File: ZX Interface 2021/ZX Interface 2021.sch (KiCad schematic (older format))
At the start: 44 parts, among them J1 AJS #1, J2 AJS #2, J3 SWAP_ROMS, J4 Cartridge, SW1 RESET, U1 74LS245, U2 74LS245, U3 74LS27, U4 74LS04, U5 27C512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

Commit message: Created proper extended cartridge symbols
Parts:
- removed U5: 27C512, Package_DIP:DIP-28_W15.24mm, symbol Memory_EPROM:27C512
- added M1, M2, M3, M4, M5, M6: Mounting, symbol mounting:Mounting
- J3: footprint (none) -> Connector_PinHeader_2.54mm:PinHeader_2x02_P2.54mm_Vertical
- J4: footprint (none) -> zx_spectrum:ZX_Spectrum_Cartridge_Port; symbol Connector_Generic:Conn_02x22_Row_Letter_Last -> zx_spectrum:cartridge_port
- U1, U2, U6: footprint (none) -> Package_DIP:DIP-20_W7.62mm_Socket_LongPads
- U3, U4: footprint (none) -> Package_DIP:DIP-14_W7.62mm_Socket_LongPads
- U7, U8: footprint (none) -> Package_DIP:DIP-16_W7.62mm_Socket_LongPads
- Z1: value ZXBUS -> ZX Spectrum; footprint (none) -> zx_spectrum:ZX_Spectrum_Expansion_Right_Angle; symbol zxbus:ZXBUS -> zx_spectrum:expansion_port
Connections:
- net labels added: EXROM, OUT_31, OUT_63
- net labels removed: Port_31, ~EXROM
- wire segments 297 -> 279
- no-connect marks 58 -> 48
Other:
- note added: "/ROM_CS is an enable for\nthe internal ZX Spectrum\nROM. Bring high to use\ncartridge."
- note added: "Sinclair Interface 2 joystick interface, but with\nAtari-style pinout (because noone wants to use\nan SJS or even have one that works properly)."
- moved on the sheet: R12, U4E

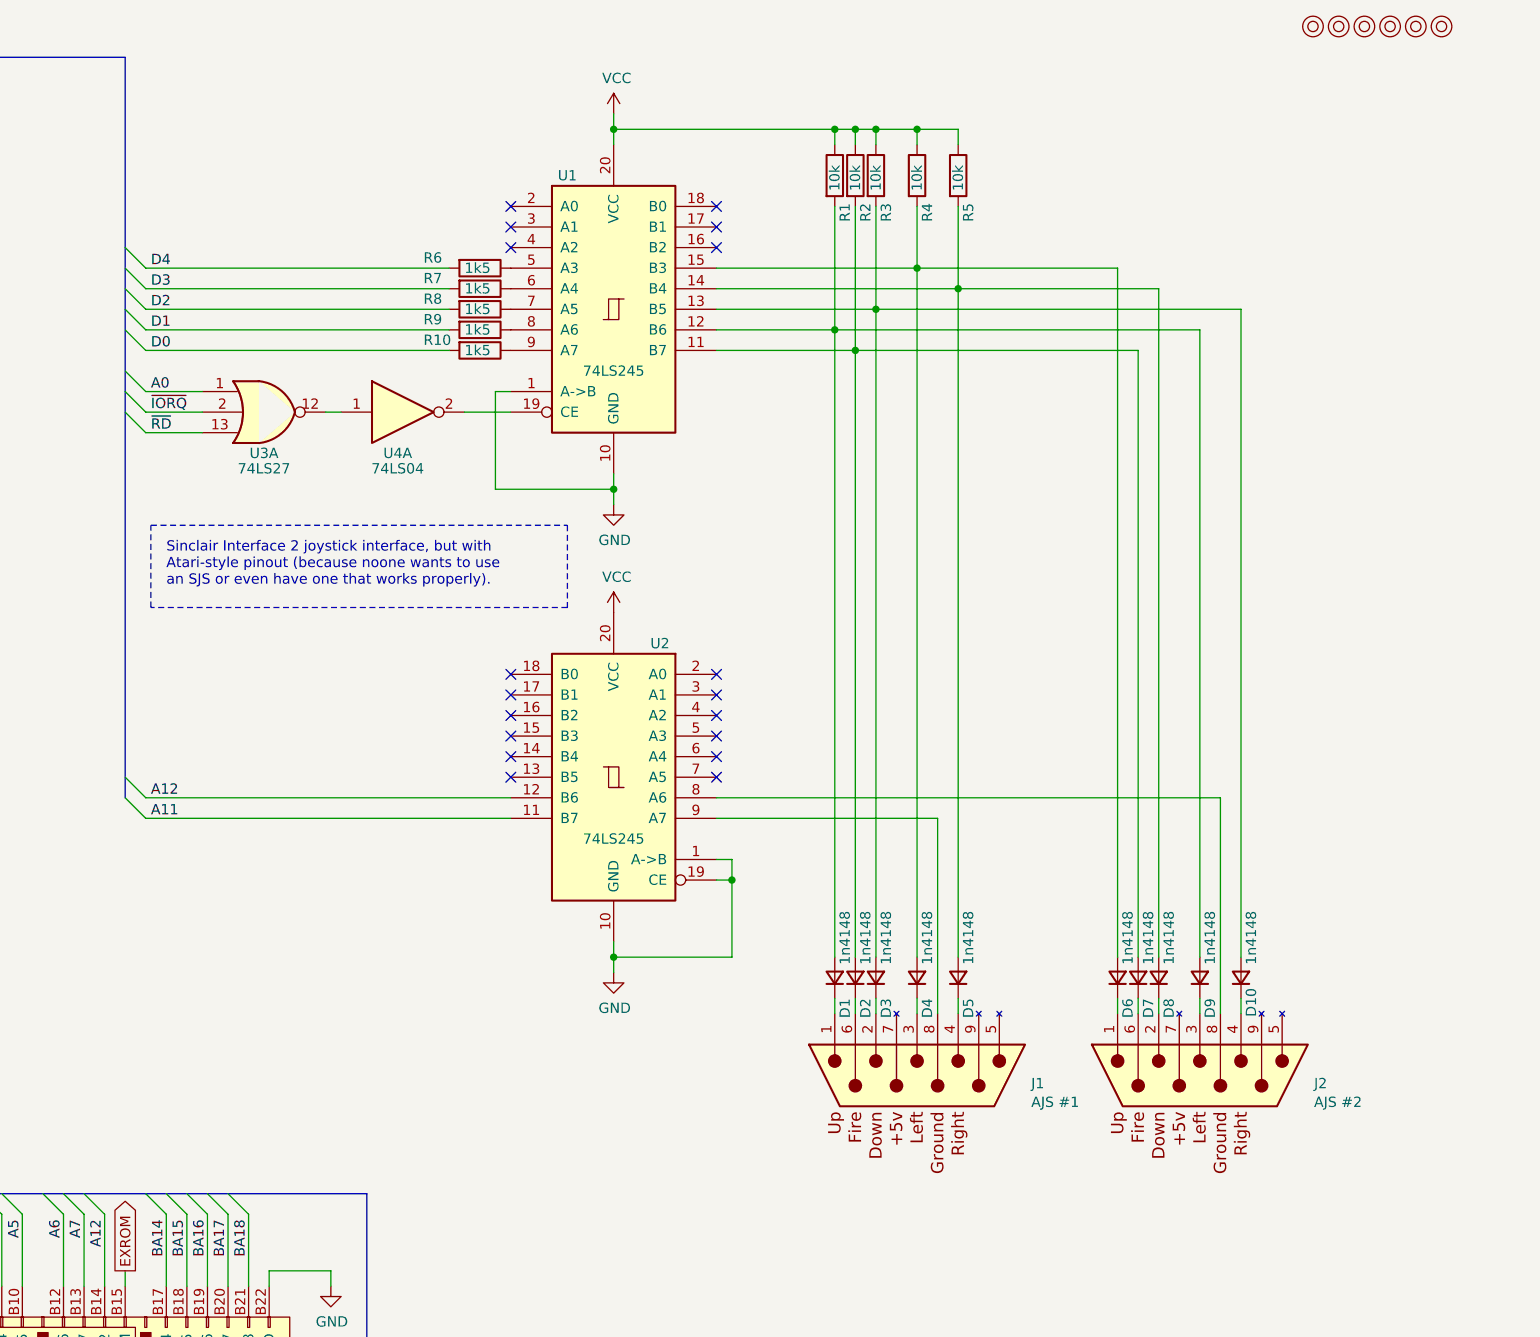
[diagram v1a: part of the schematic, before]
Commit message: Assigned footprints
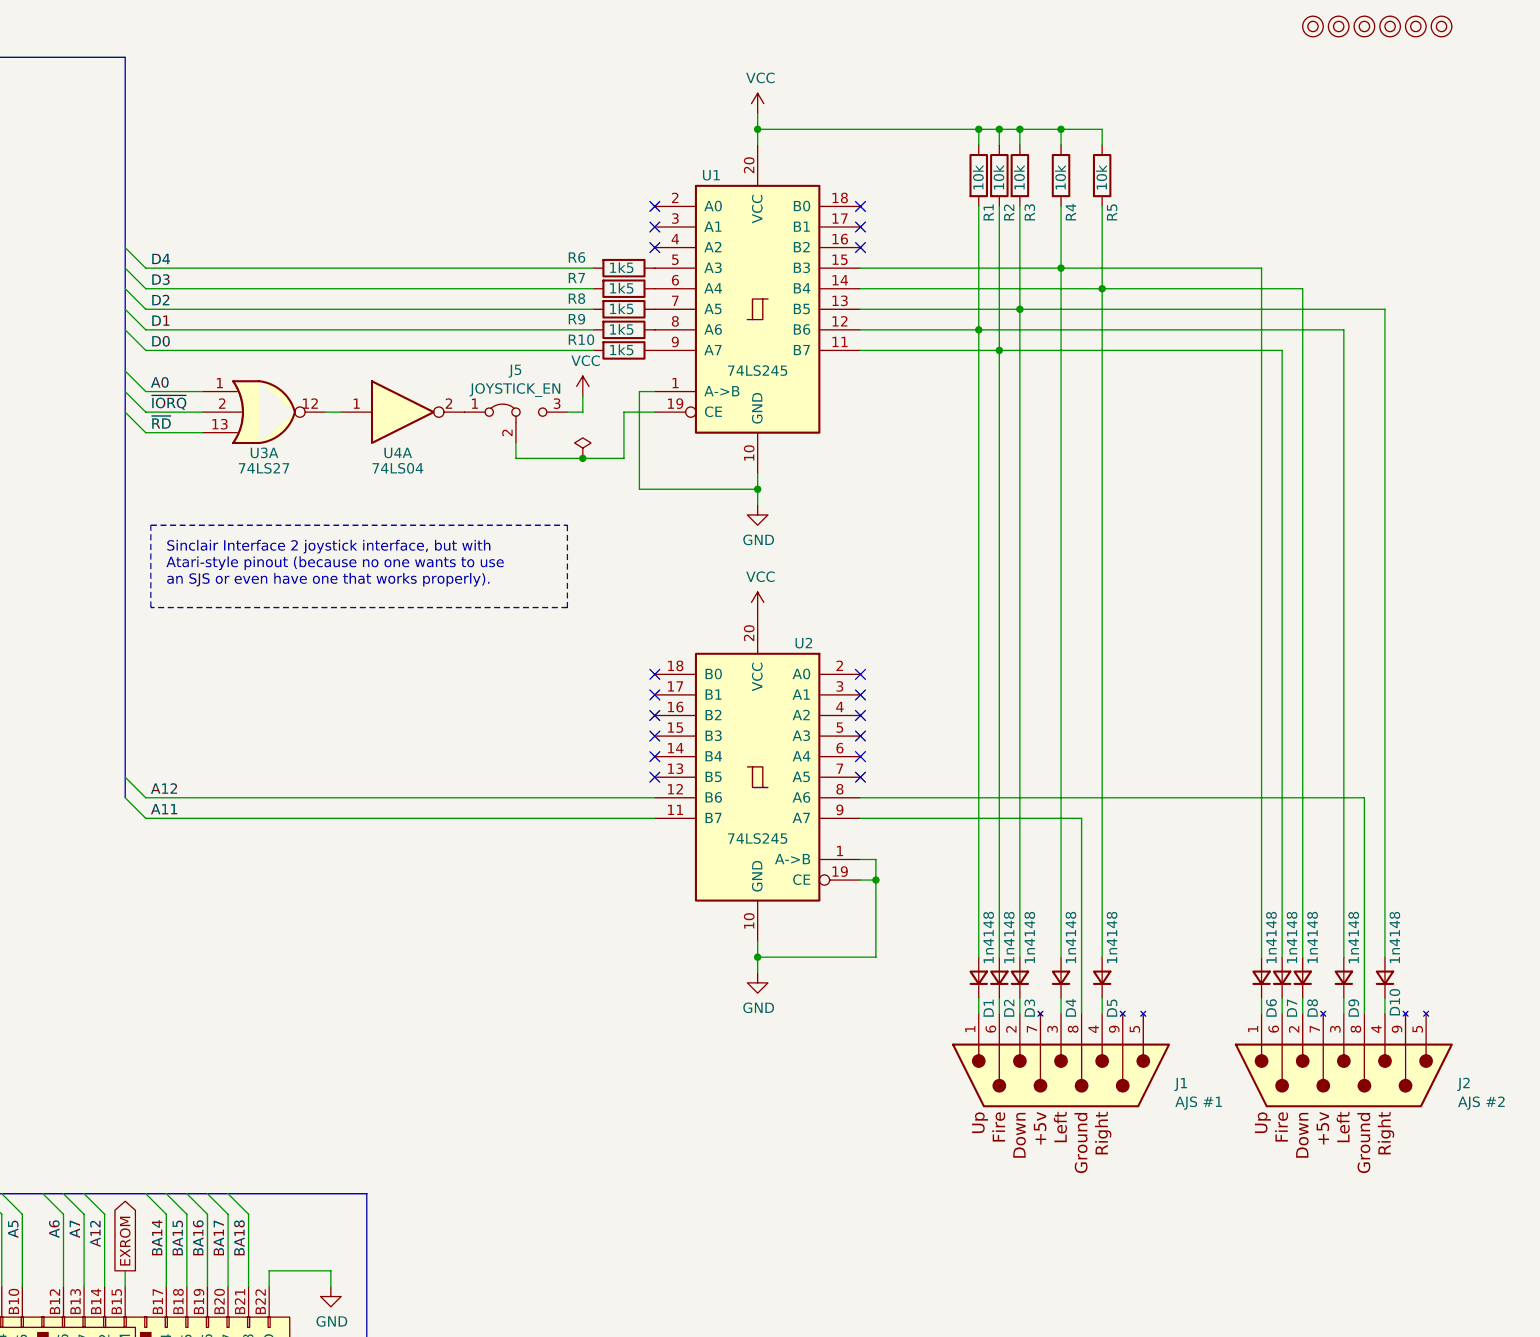
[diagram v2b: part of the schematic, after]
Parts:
- added J5: JOYSTICK_EN, Connector_PinHeader_2.54mm:PinHeader_1x03_P2.54mm_Vertical, symbol Jumper:Jumper_3_Bridged12
- D1, D10, D2, D3, D4, D5, D6, D7, D8, D9: footprint (none) -> Diode_THT:D_DO-35_SOD27_P7.62mm_Horizontal
- J1, J2: footprint (none) -> RND_DSUB:DSUB-9_Male_Vertical_Pitch2.77x2.84mm
- M1, M2, M3, M4, M5, M6: footprint (none) -> mounting:M3_pin
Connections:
- net VCC: now also J5.3 (B)
- net at U1.19 (CE): now also J5.2 (C); no longer U4.2
- new net: J5.1 (A), U4.2
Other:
- note added: "Sinclair Interface 2 joystick interface, but with\nAtari-style pinout (because no one wants to use\nan SJS or even have one that works properly)."
- note removed: "Sinclair Interface 2 joystick interface, but with\nAtari-style pinout (because noone wants to use\nan SJS or even have one that works properly)."
- moved on the sheet: D1, D10, D2, D3, D4, D5, D6, D7, D8, D9, J1, J2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

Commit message: Laying some tracks...
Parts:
- D1, D10, D2, D3, D4, D5, D6, D7, D8, D9: footprint Diode_THT:D_DO-35_SOD27_P7.62mm_Horizontal -> 1n4148:D_DO-35_SOD27_P7.62mm_Horizontal
- SW1: footprint Button_Switch_THT:SW_PUSH_6mm_H13mm -> switch_cutout:SW_PUSH_6mm
- Z1: footprint zx_spectrum:ZX_Spectrum_Expansion_Right_Angle -> zx_spectrum:ZX_Spectrum_Expansion_Edge
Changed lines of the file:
@@
 F 0 "Z1" H 2400 7776 39  0000 C CNN
 F 1 "ZX Spectrum" H 2400 7701 39  0000 C CNN
-F 2 "zx_spectrum:ZX_Spectrum_Expansion_Right_Angle" H 2050 4375 39  0001 C CNN
+F 2 "zx_spectrum:ZX_Spectrum_Expansion_Edge" H 2050 4375 39  0001 C CNN
 F 3 "" H 2050 4375 39  0001 C CNN
 	1    2050 4375
@@
 F 0 "D1" H 13625 5125 50  0000 R CNN
 F 1 "1n4148" H 14050 5125 50  0000 R CNN
-F 2 "Diode_THT:D_DO-35_SOD27_P7.62mm_Horizontal" V 13725 5175 50  0001 C CNN
+F 2 "1n4148:D_DO-35_SOD27_P7.62mm_Horizontal" V 13725 5175 50  0001 C CNN
 F 3 "~" V 13725 5175 50  0001 C CNN
 	1    13725 5175
@@
 F 0 "D2" H 13725 5125 50  0000 R CNN
 F 1 "1n4148" H 14150 5125 50  0000 R CNN
-F 2 "Diode_THT:D_DO-35_SOD27_P7.62mm_Horizontal" V 13825 5175 50  0001 C CNN
+F 2 "1n4148:D_DO-35_SOD27_P7.62mm_Horizontal" V 13825 5175 50  0001 C CNN
 F 3 "~" V 13825 5175 50  0001 C CNN
 	1    13825 5175
@@
 F 0 "D3" H 13825 5125 50  0000 R CNN
 F 1 "1n4148" H 14250 5125 50  0000 R CNN
-F 2 "Diode_THT:D_DO-35_SOD27_P7.62mm_Horizontal" V 13925 5175 50  0001 C CNN
+F 2 "1n4148:D_DO-35_SOD27_P7.62mm_Horizontal" V 13925 5175 50  0001 C CNN
 F 3 "~" V 13925 5175 50  0001 C CNN
 	1    13925 5175
@@
 F 0 "D4" H 14025 5125 50  0000 R CNN
 F 1 "1n4148" H 14450 5125 50  0000 R CNN
-F 2 "Diode_THT:D_DO-35_SOD27_P7.62mm_Horizontal" V 14125 5175 50  0001 C CNN
+F 2 "1n4148:D_DO-35_SOD27_P7.62mm_Horizontal" V 14125 5175 50  0001 C CNN
 F 3 "~" V 14125 5175 50  0001 C CNN
 	1    14125 5175
@@
 F 0 "D5" H 14225 5125 50  0000 R CNN
 F 1 "1n4148" H 14650 5125 50  0000 R CNN
-F 2 "Diode_THT:D_DO-35_SOD27_P7.62mm_Horizontal" V 14325 5175 50  0001 C CNN
+F 2 "1n4148:D_DO-35_SOD27_P7.62mm_Horizontal" V 14325 5175 50  0001 C CNN
 F 3 "~" V 14325 5175 50  0001 C CNN
 	1    14325 5175
@@
 F 0 "D6" H 15000 5125 50  0000 R CNN
 F 1 "1n4148" H 15425 5125 50  0000 R CNN
-F 2 "Diode_THT:D_DO-35_SOD27_P7.62mm_Horizontal" V 15100 5175 50  0001 C CNN
+F 2 "1n4148:D_DO-35_SOD27_P7.62mm_Horizontal" V 15100 5175 50  0001 C CNN
 F 3 "~" V 15100 5175 50  0001 C CNN
 	1    15100 5175
@@
 F 0 "D7" H 15100 5125 50  0000 R CNN
 F 1 "1n4148" H 15525 5125 50  0000 R CNN
-F 2 "Diode_THT:D_DO-35_SOD27_P7.62mm_Horizontal" V 15200 5175 50  0001 C CNN
+F 2 "1n4148:D_DO-35_SOD27_P7.62mm_Horizontal" V 15200 5175 50  0001 C CNN
 F 3 "~" V 15200 5175 50  0001 C CNN
 	1    15200 5175
@@
 F 0 "D8" H 15200 5125 50  0000 R CNN
 F 1 "1n4148" H 15625 5125 50  0000 R CNN
-F 2 "Diode_THT:D_DO-35_SOD27_P7.62mm_Horizontal" V 15300 5175 50  0001 C CNN
+F 2 "1n4148:D_DO-35_SOD27_P7.62mm_Horizontal" V 15300 5175 50  0001 C CNN
 F 3 "~" V 15300 5175 50  0001 C CNN
 	1    15300 5175
@@
 F 0 "D9" H 15400 5125 50  0000 R CNN
 F 1 "1n4148" H 15825 5125 50  0000 R CNN
-F 2 "Diode_THT:D_DO-35_SOD27_P7.62mm_Horizontal" V 15500 5175 50  0001 C CNN
+F 2 "1n4148:D_DO-35_SOD27_P7.62mm_Horizontal" V 15500 5175 50  0001 C CNN
 F 3 "~" V 15500 5175 50  0001 C CNN
 	1    15500 5175
@@
 F 0 "D10" H 15650 5125 50  0000 R CNN
 F 1 "1n4148" H 16025 5125 50  0000 R CNN
-F 2 "Diode_THT:D_DO-35_SOD27_P7.62mm_Horizontal" V 15700 5175 50  0001 C CNN
+F 2 "1n4148:D_DO-35_SOD27_P7.62mm_Horizontal" V 15700 5175 50  0001 C CNN
 F 3 "~" V 15700 5175 50  0001 C CNN
 	1    15700 5175
@@
 F 0 "SW1" H 5325 6185 50  0000 C CNN
 F 1 "RESET" H 5325 6094 50  0000 C CNN
-F 2 "Button_Switch_THT:SW_PUSH_6mm_H13mm" H 5325 6100 50  0001 C CNN
+F 2 "switch_cutout:SW_PUSH_6mm" H 5325 6100 50  0001 C CNN
 F 3 "~" H 5325 6100 50  0001 C CNN
 	1    5325 5900
@@
 Wire Wire Line
 	12000 2425 12150 2425
-Wire Bus Line
-	8275 8300 10750 8300
-Wire Bus Line
-	7575 6225 10750 6225
-Wire Bus Line
-	3450 700  3450 3975
-Wire Bus Line
-	6200 5800 6200 10850
-Wire Bus Line
-	1475 700  1475 10850
-Wire Bus Line
-	9575 700  9575 4300
 $Comp
 L power:PWR_FLAG #FLG0101
@@
 	1    0    0    -1
 $EndComp
+Wire Bus Line
+	9575 700  9575 4300
+Wire Bus Line
+	6200 5800 6200 10850
+Wire Bus Line
+	3450 700  3450 3975
+Wire Bus Line
+	7575 6225 10750 6225
+Wire Bus Line
+	8275 8300 10750 8300
+Wire Bus Line
+	1475 700  1475 10850
 $EndSCHEMATC

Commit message: ... and the rest
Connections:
- net ~ROM_0: now also J4.A18 (~ROM_0); no longer J4.A20 (~ROM_2)
- net ~ROM_2: now also J4.A20 (~ROM_2); no longer J4.A18 (~ROM_0)
- net ~ROM_3: now also J4.A21 (~ROM_3); no longer J4.A17 (~ROM_OE)
- net ~ROM_OE: now also J4.A17 (~ROM_OE); no longer J4.A21 (~ROM_3)
- net IF2_EN renamed CARTRIDGE_EN
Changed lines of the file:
@@
 	1    0    0    -1
 $EndComp
-Text Label 2875 7500 0    50   ~ 0
-IF2_EN
+Text Label 2925 8800 3    50   ~ 0
+CARTRIDGE_EN
 $Comp
 L power:VCC #PWR0111
@@
 Text Label 10175 6350 3    50   ~ 0
 BA18
-Text Label 9775 8175 1    50   ~ 0
+Text Label 10175 8175 1    50   ~ 0
 ~ROM_3
-Text Label 9875 8175 1    50   ~ 0
+Text Label 10075 8175 1    50   ~ 0
 ~ROM_2
 Text Label 9975 8175 1    50   ~ 0
 ~ROM_1
-Text Label 10075 8175 1    50   ~ 0
+Text Label 9875 8175 1    50   ~ 0
 ~ROM_0
 Text Label 8475 6350 3    50   ~ 0
@@
 Wire Wire Line
 	10175 6325 10175 6675
-Text Label 10175 8175 1    50   ~ 0
+Text Label 9775 8175 1    50   ~ 0
 ~ROM_OE
 Text GLabel 9575 6600 1    50   Output ~ 0
